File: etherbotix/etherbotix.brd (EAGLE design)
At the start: 100 x 50 mm, 107 parts, among them J1 J3011G21DNL, J2 22-03-5035, J3 22-03-5035, J4 22-03-5045, J5 22-03-5045, J6 1760510000, J7 1760490000, J8 502443-0470, J9 502443-0470, T1 TESTPAD, T2 TESTPAD, T3 TESTPAD, T4 TESTPAD, T5 TESTPAD, T6 TESTPAD, U1 STM32F407V, U2 TLK110, U3 OKI-78SR-5, U4 TLV1117, U5 ACS711ELCTR-25AB-T, U6 ACS711ELCTR-25AB-T, U7 MAX481CSA, U8 74LS126D, X1 25MHZ

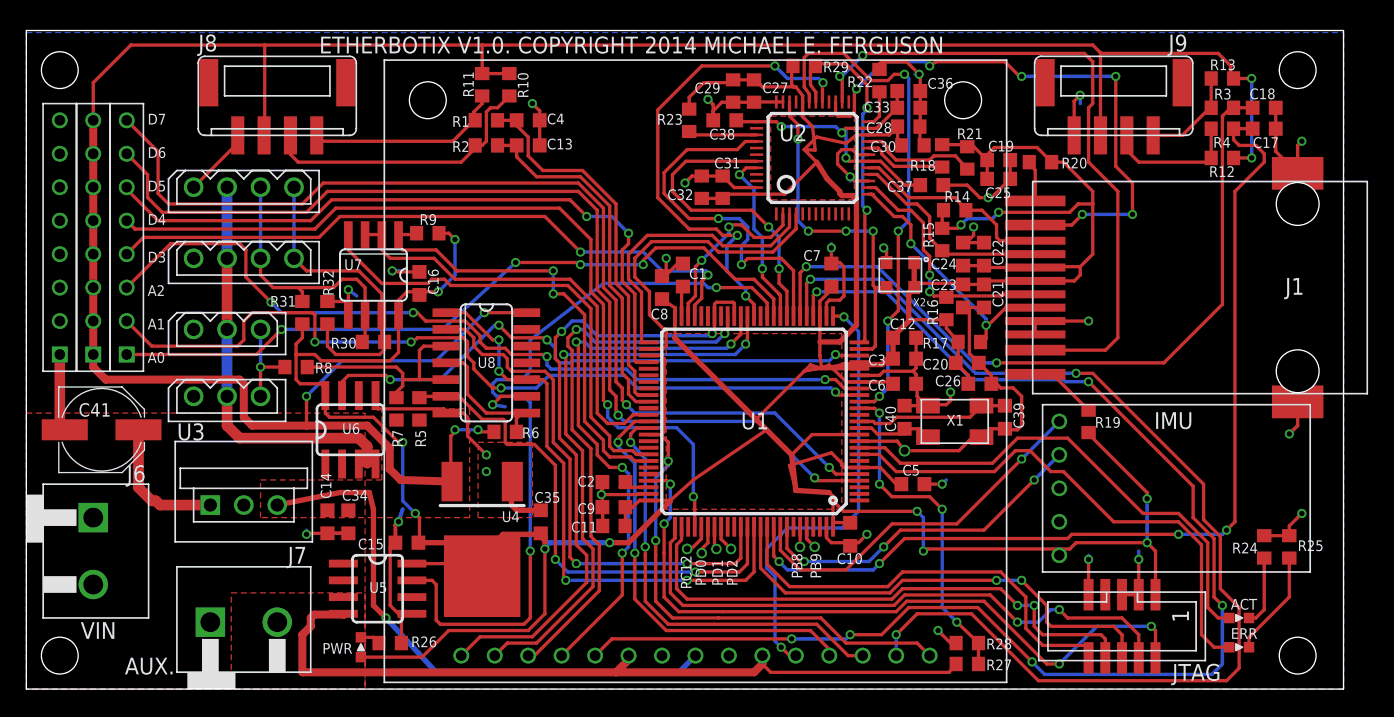
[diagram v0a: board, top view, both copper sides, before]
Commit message: move imu slightly down
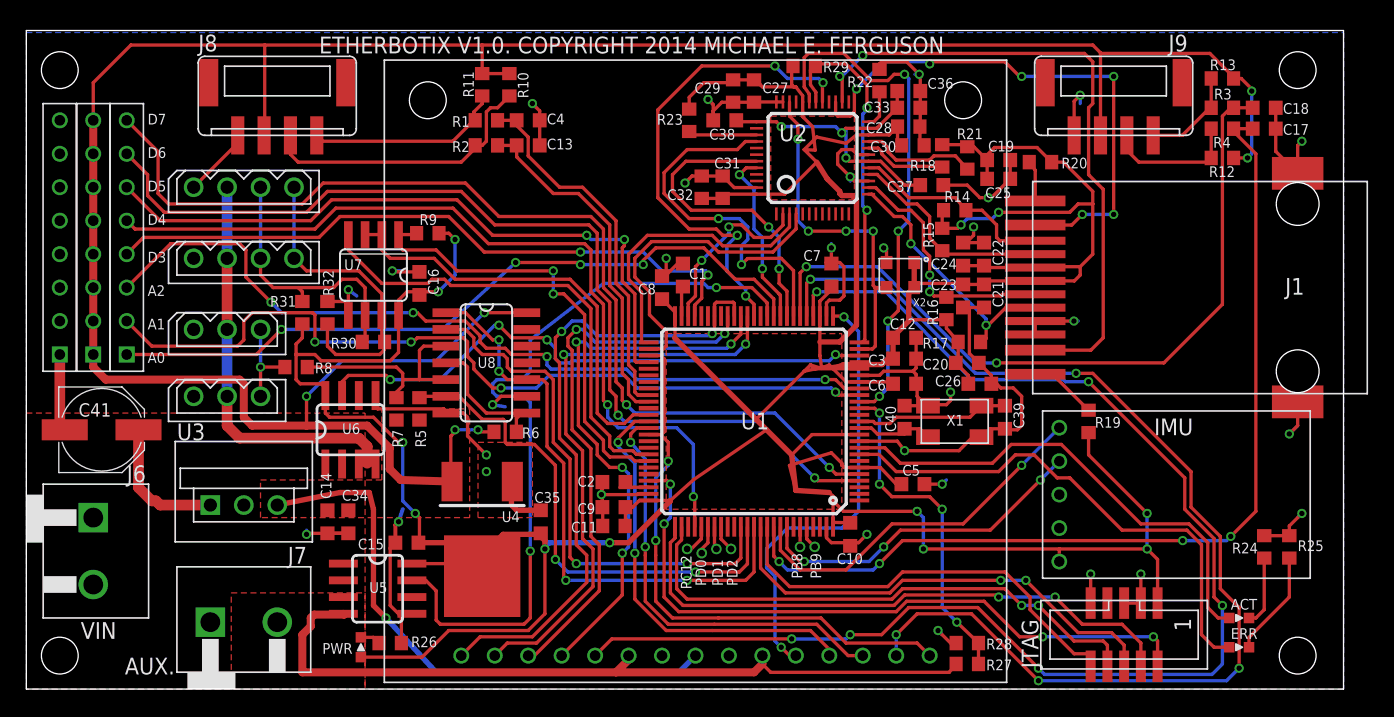
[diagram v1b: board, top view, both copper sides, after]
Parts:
- moved JTAG 0.65 mm to (83.3, 4.13)
- moved IMU 0.48 mm to (78.4, 14.8)
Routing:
- net GND: track 207.7 -> 204.8 mm
- net TMS: track 54.4 -> 52.4 mm
- net N$18: track 46.3 -> 44.2 mm
- net N$20: track 50.9 -> 49.3 mm
- net D6: track 76.4 -> 75.3 mm
- net +5V: track 241.7 -> 240.7 mm
- net D7: track 77.6 -> 76.7 mm
- net M2_ENC_B: track 73.1 -> 72.3 mm
- net M1_ENC_B: track 27.6 -> 26.7 mm
- net D5: track 52.3 -> 51.5 mm
- net M1_ENC_A: track 28.7 -> 28.0 mm
- net VCC: track 360.4 -> 361.0 mm
- net M2_A: vias 3 -> 5

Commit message: some more refinements
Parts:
- moved C16 0.16 mm to (29.8, 31.0)
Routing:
- net M2_SENSE: track 33.5 -> 44.3 mm, vias 2 -> 4
- net N$18: track 44.2 -> 35.5 mm, vias 6 -> 4
- net M2_ENC_A: track 57.2 -> 54.0 mm
- net VCC: track 361.0 -> 358.7 mm
- net +5V: track 240.7 -> 242.1 mm
- net M2_ENC_B: track 72.3 -> 73.5 mm, vias 4 -> 2
- net AUX_CURRENT_SENSE: track 58.7 -> 59.9 mm, vias 2 -> 4
- net A0: track 55.6 -> 56.5 mm, vias 4 -> 6
- net D3: track 50.8 -> 51.7 mm
- net GND: track 204.8 -> 204.1 mm
- net M2_EN: track 43.9 -> 44.4 mm
- net V_SENSE: track 25.5 -> 25.0 mm
- net M2_B: track 32.9 -> 33.4 mm

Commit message: some more refinements
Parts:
- moved R23 0.16 mm to (50.3, 43.3)
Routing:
- net ETH_CLK: track 27.1 -> 24.2 mm, vias 4 -> 2
- net GND: track 204.1 -> 202.8 mm
- net N$24: track 23.9 -> 23.3 mm

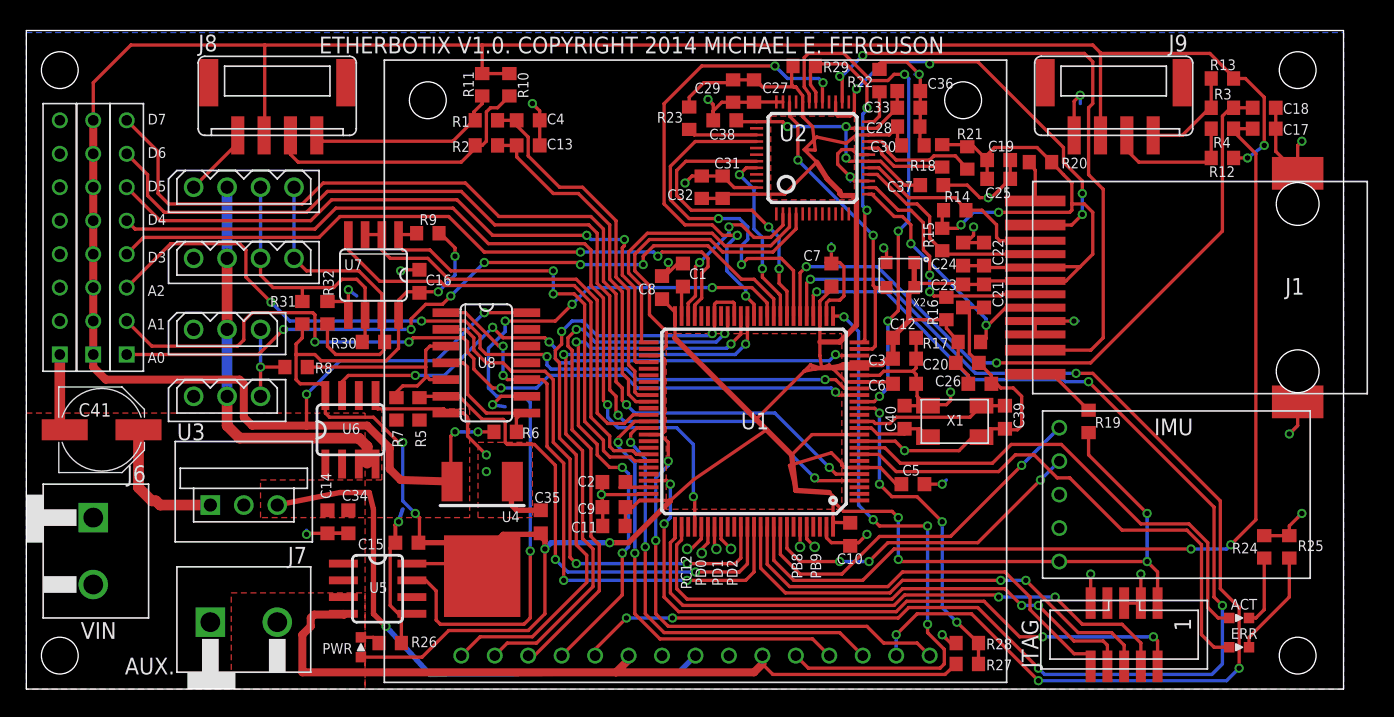
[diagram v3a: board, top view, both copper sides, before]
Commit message: add estop-capable 3-pin VIN header
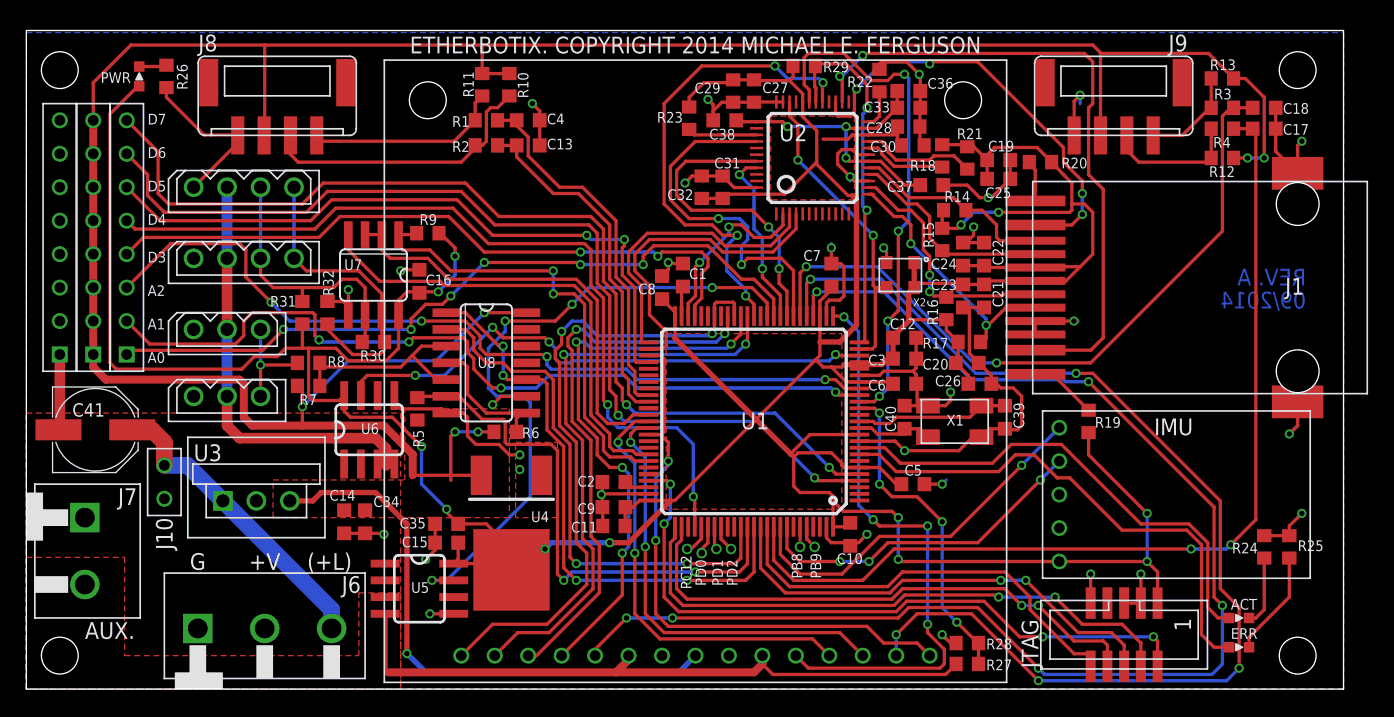
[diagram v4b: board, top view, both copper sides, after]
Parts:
- added J10: JUMPER, headers:J2
- J6: value 1760510000 -> 1760520000; device headers:1760490000 -> headers:1760520000
- moved PWR 46.5 mm to (8.57, 46.5)
- moved R26 46.3 mm to (10.6, 46.5), turned to 90 degrees
- moved J7 12.4 mm to (4.45, 13.0), turned to 270 degrees
- moved J6 11.6 mm to (13.0, 4.60), turned to 0 degrees
- moved C35 7.15 mm to (31.9, 12.5), turned to 180 degrees
- moved R7 6.89 mm to (21.4, 23.0), turned to 180 degrees
- moved U5 3.17 mm to (29.8, 7.62)
- moved C15 3.02 mm to (31.9, 11.1)
- moved U4 2.27 mm to (36.8, 9.05)
- moved U6 1.43 mm to (26.0, 19.7)
- moved C14 1.27 mm to (24.1, 12.7)
- moved C34 1.27 mm to (25.7, 12.7)
- moved R8 1.00 mm to (21.4, 24.8)
- moved U3 1.00 mm to (17.5, 14.3)
- moved C41 0.48 mm to (5.24, 19.7)
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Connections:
- new net N$29: C41.+, J10.B, J6.3, U3.P$1
- net +12V: now also J10.A; no longer C41.+, U3.P$1
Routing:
- net N$29: track 0.00 -> 23.2 mm
- net GND: track 202.8 -> 190.2 mm, vias 30 -> 31
- net +12V: track 10.4 -> 0.00 mm
- net AUX_CURRENT_SENSE: track 59.9 -> 50.5 mm
- net +12V-AUX: track 60.0 -> 50.7 mm
- net +5V: track 242.1 -> 245.9 mm
- net VCC: track 358.5 -> 356.0 mm
- net N$12: track 17.4 -> 15.4 mm
- net USART2_RX: track 38.6 -> 40.6 mm
- net N$2: track 32.6 -> 34.1 mm
- net SERVO_CURRENT_SENSE: track 43.9 -> 42.5 mm
- net N$14: track 6.93 -> 7.93 mm
- net N$11: track 23.9 -> 23.2 mm
- net A1: track 64.1 -> 63.5 mm
- net M2_ENC_B: track 73.5 -> 72.9 mm
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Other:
- board text added: "(+L)"
- board text added: "+V"
- board text added: "09/2014"
- board text added: "ETHERBOTIX. COPYRIGHT 2014 MICHAEL E. FERGUSON"
- board text added: "G"
- board text added: "J10"
- board text added: "REV. A"
- board text removed: "ETHERBOTIX V1.0. COPYRIGHT 2014 MICHAEL E. FERGUSON"
- board text removed: "VIN"

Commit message: add top-side ground plane
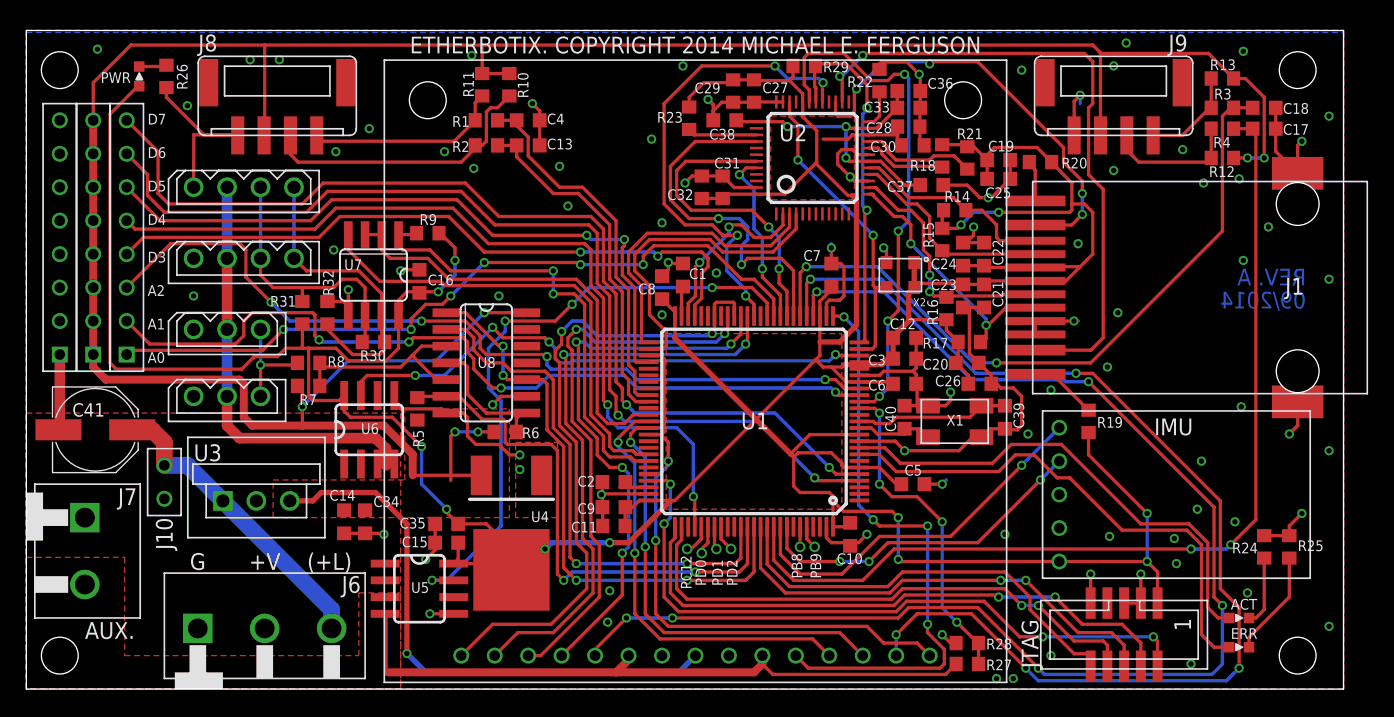
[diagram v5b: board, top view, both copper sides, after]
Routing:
- net AUX_CURRENT_SENSE: track 50.5 -> 47.5 mm
- net GND: track 190.2 -> 192.2 mm, vias 31 -> 84

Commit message: nearly done with layout
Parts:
- moved U4 0.48 mm to (37.3, 9.05)
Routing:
- net USART2_WE: track 44.2 -> 43.7 mm
- net GND: track 192.2 -> 191.8 mm, vias 84 -> 85

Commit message: final rev. A updates
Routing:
- net +12V-AUX: track 50.7 -> 51.9 mm
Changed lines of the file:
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@@
 </element>
 <element name="C3" library="fergs" package="C0603" value="0.1uF" x="66.675" y="25.0825" smashed="yes">
-<attribute name="NAME" x="65.2525" y="25.385" size="0.8128" layer="25" rot="R180"/>
+<attribute name="NAME" x="65.2525" y="25.385" size="0.6096" layer="25" rot="R180"/>
 <attribute name="VALUE" x="65.875" y="23.4325" size="1.016" layer="27"/>
 </element>
@@
 </element>
 <element name="C6" library="fergs" package="C0603" value="0.1uF" x="66.675" y="23.1775" smashed="yes">
-<attribute name="NAME" x="65.2525" y="23.48" size="0.8128" layer="25" rot="R180"/>
+<attribute name="NAME" x="65.2525" y="23.48" size="0.6096" layer="25" rot="R180"/>
 <attribute name="VALUE" x="65.875" y="21.5275" size="1.016" layer="27"/>
 </element>
@@
 </element>
 <element name="C17" library="fergs" package="C0603" value="100pF" x="93.98" y="42.545" smashed="yes">
-<attribute name="NAME" x="95.4025" y="42.08375" size="0.8128" layer="25"/>
+<attribute name="NAME" x="95.56125" y="42.08375" size="0.8128" layer="25"/>
 <attribute name="VALUE" x="93.18" y="40.895" size="1.016" layer="27"/>
 </element>
 <element name="C18" library="fergs" package="C0603" value="100pF" x="93.98" y="44.1325" smashed="yes">
-<attribute name="NAME" x="95.4025" y="43.67125" size="0.8128" layer="25"/>
+<attribute name="NAME" x="95.56125" y="43.67125" size="0.8128" layer="25"/>
 <attribute name="VALUE" x="93.18" y="42.4825" size="1.016" layer="27"/>
 </element>
@@
 </element>
 <element name="R14" library="fergs" package="0603" value="49R9" x="70.485" y="36.35375" smashed="yes">
-<attribute name="NAME" x="69.69125" y="36.98875" size="0.8128" layer="25"/>
+<attribute name="NAME" x="69.85" y="36.98875" size="0.6096" layer="25"/>
 <attribute name="VALUE" x="69.85" y="34.44875" size="1.27" layer="27"/>
 </element>
@@
 </element>
 <element name="R17" library="fergs" package="0603" value="49R9" x="71.59625" y="26.3525" smashed="yes" rot="R180">
-<attribute name="NAME" x="70.00875" y="26.67" size="0.8128" layer="25" rot="R180"/>
+<attribute name="NAME" x="70.00875" y="26.67" size="0.6096" layer="25" rot="R180"/>
 <attribute name="VALUE" x="72.23125" y="28.2575" size="1.27" layer="27" rot="R180"/>
 </element>
@@
 </element>
 <element name="C20" library="fergs" package="C0603" value="1uF" x="71.4375" y="24.765" smashed="yes">
-<attribute name="NAME" x="70.015" y="25.0675" size="0.8128" layer="25" rot="R180"/>
+<attribute name="NAME" x="70.015" y="25.0675" size="0.6096" layer="25" rot="R180"/>
 <attribute name="VALUE" x="70.6375" y="23.115" size="1.016" layer="27"/>
 </element>
@@
 </element>
 <element name="C26" library="fergs" package="C0603" value="0.1uF" x="72.39" y="23.1775" smashed="yes">
-<attribute name="NAME" x="70.9675" y="23.7975" size="0.8128" layer="25" rot="R180"/>
+<attribute name="NAME" x="70.9675" y="23.7975" size="0.6096" layer="25" rot="R180"/>
 <attribute name="VALUE" x="71.59" y="21.5275" size="1.016" layer="27"/>
 </element>
@@
 </element>
 <element name="C31" library="fergs" package="0603" value="4.7uF" x="52.86375" y="38.1" smashed="yes" rot="R90">
-<attribute name="NAME" x="52.22875" y="39.52875" size="0.8128" layer="25"/>
+<attribute name="NAME" x="52.07" y="39.52875" size="0.8128" layer="25"/>
 <attribute name="VALUE" x="54.76875" y="37.465" size="1.27" layer="27" rot="R90"/>
 </element>
@@
 </element>
 <element name="R24" library="fergs" package="0603" value="1k" x="93.98" y="10.795" smashed="yes" rot="R270">
-<attribute name="NAME" x="93.50375" y="11.1125" size="0.8128" layer="25" rot="R180"/>
+<attribute name="NAME" x="94.45625" y="12.3825" size="0.8128" layer="25" rot="R90"/>
 <attribute name="VALUE" x="92.075" y="11.43" size="1.27" layer="27" rot="R270"/>
 </element>
 <element name="R25" library="fergs" package="0603" value="1k" x="95.885" y="10.795" smashed="yes" rot="R270">
-<attribute name="NAME" x="96.52" y="10.4775" size="0.8128" layer="25"/>
+<attribute name="NAME" x="96.2025" y="12.3825" size="0.8128" layer="25" rot="R90"/>
 <attribute name="VALUE" x="93.98" y="11.43" size="1.27" layer="27" rot="R270"/>
 </element>
@@
 </element>
 <element name="R27" library="fergs" package="0603" value="15k" x="71.4375" y="1.905" smashed="yes" rot="R180">
-<attribute name="NAME" x="72.86625" y="1.42875" size="0.8128" layer="25"/>
+<attribute name="NAME" x="73.81875" y="1.27" size="0.8128" layer="25" rot="R90"/>
 <attribute name="VALUE" x="72.0725" y="3.81" size="1.27" layer="27" rot="R180"/>
 </element>
 <element name="R28" library="fergs" package="0603" value="1k" x="71.4375" y="3.4925" smashed="yes">
-<attribute name="NAME" x="72.86625" y="3.01625" size="0.8128" layer="25"/>
+<attribute name="NAME" x="71.12" y="4.1275" size="0.8128" layer="25"/>
 <attribute name="VALUE" x="70.8025" y="1.5875" size="1.27" layer="27"/>
 </element>
@@
 <contactref element="MOTORS" pad="VIN1"/>
 <contactref element="MOTORS" pad="VIN2"/>
-<wire x1="45.72" y1="2.54" x2="45.72" y2="2.2225" width="0.6096" layer="1"/>
-<wire x1="45.72" y1="2.2225" x2="44.7675" y2="1.27" width="0.6096" layer="1"/>
-<wire x1="44.7675" y1="1.27" x2="27.46375" y2="1.27" width="0.6096" layer="1"/>
-<wire x1="55.88" y1="2.54" x2="55.88" y2="1.905" width="0.6096" layer="1"/>
-<wire x1="55.88" y1="1.905" x2="55.245" y2="1.27" width="0.6096" layer="1"/>
-<wire x1="55.245" y1="1.27" x2="44.7675" y2="1.27" width="0.6096" layer="1"/>
+<wire x1="45.72" y1="2.54" x2="45.72" y2="2.2225" width="0.8128" layer="1"/>
+<wire x1="45.72" y1="2.2225" x2="44.29125" y2="0.79375" width="0.8128" layer="1"/>
+<wire x1="44.29125" y1="0.79375" x2="26.9875" y2="0.79375" width="0.8128" layer="1"/>
+<wire x1="55.88" y1="2.54" x2="54.13375" y2="0.79375" width="0.8128" layer="1"/>
+<wire x1="54.13375" y1="0.79375" x2="44.29125" y2="0.79375" width="0.8128" layer="1"/>
 <contactref element="R27" pad="2"/>
-<wire x1="55.88" y1="1.905" x2="56.67375" y2="1.11125" width="0.254" layer="1"/>
-<wire x1="56.67375" y1="1.11125" x2="69.79375" y2="1.11125" width="0.254" layer="1"/>
 <wire x1="27.305" y1="1.42875" x2="27.305" y2="5.655" width="0.254" layer="1"/>
 <wire x1="27.305" y1="5.655" x2="27.245" y2="5.715" width="0.254" layer="1"/>
 <wire x1="69.79375" y1="1.11125" x2="70.5875" y2="1.905" width="0.254" layer="1"/>
+<wire x1="69.79375" y1="1.11125" x2="57.30875" y2="1.11125" width="0.254" layer="1"/>
+<wire x1="57.30875" y1="1.11125" x2="55.88" y2="2.54" width="0.254" layer="1"/>
 </signal>
 <signal name="AUX_CURRENT_SENSE">

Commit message: start rev. B
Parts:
- added T7, T8, T9: TESTPAD, fergs:TEST
- moved R1 1.60 mm to (36.5, 43.0)
- moved R2 1.60 mm to (36.5, 41.1)
- moved C13 1.60 mm to (39.7, 43.0)
- moved C4 1.60 mm to (39.7, 41.1)
- moved R10 1.60 mm to (38.3, 45.7)
- moved R11 1.60 mm to (36.2, 45.7)
- moved C10 0.95 mm to (63.5, 11.7)
- moved T1 0.79 mm to (59.4, 10.2)
- moved C5 0.35 mm to (67.5, 15.9)
- moved T2 0.29 mm to (58.4, 10.8)
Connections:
- new net PE0: T7.T, U1.97
- new net PE1: T8.T, U1.98
- new net PE4: T9.T, U1.3
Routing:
- net PE1: track 0.00 -> 2.81 mm
- net PE0: track 0.00 -> 2.47 mm
- net PE4: track 0.00 -> 2.20 mm
- net M1_ENC_B: track 26.7 -> 25.1 mm
- net M1_ENC_A: track 28.0 -> 26.3 mm
- net N$6: track 21.9 -> 23.4 mm
- net N$7: track 14.9 -> 16.5 mm
- net VCC: track 356.2 -> 357.2 mm
- net GND: track 191.8 -> 192.7 mm
- net I2C1_SCL: track 28.1 -> 28.9 mm
- net I2C1_SDA: track 25.9 -> 26.5 mm
- net M2_ENC_B: track 72.6 -> 73.2 mm
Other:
- board text added: "PE0"
- board text added: "PE1"
- board text added: "PE4"
- board text added: "REV. B"
- board text removed: "REV. A"
